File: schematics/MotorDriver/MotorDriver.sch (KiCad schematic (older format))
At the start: 13 parts, among them J1 I2C, J2 UART, J3 3V3IN, J4 9VIN, U1 ATmega328P-PU, U2 TB6612FNG, Y1 16MHz

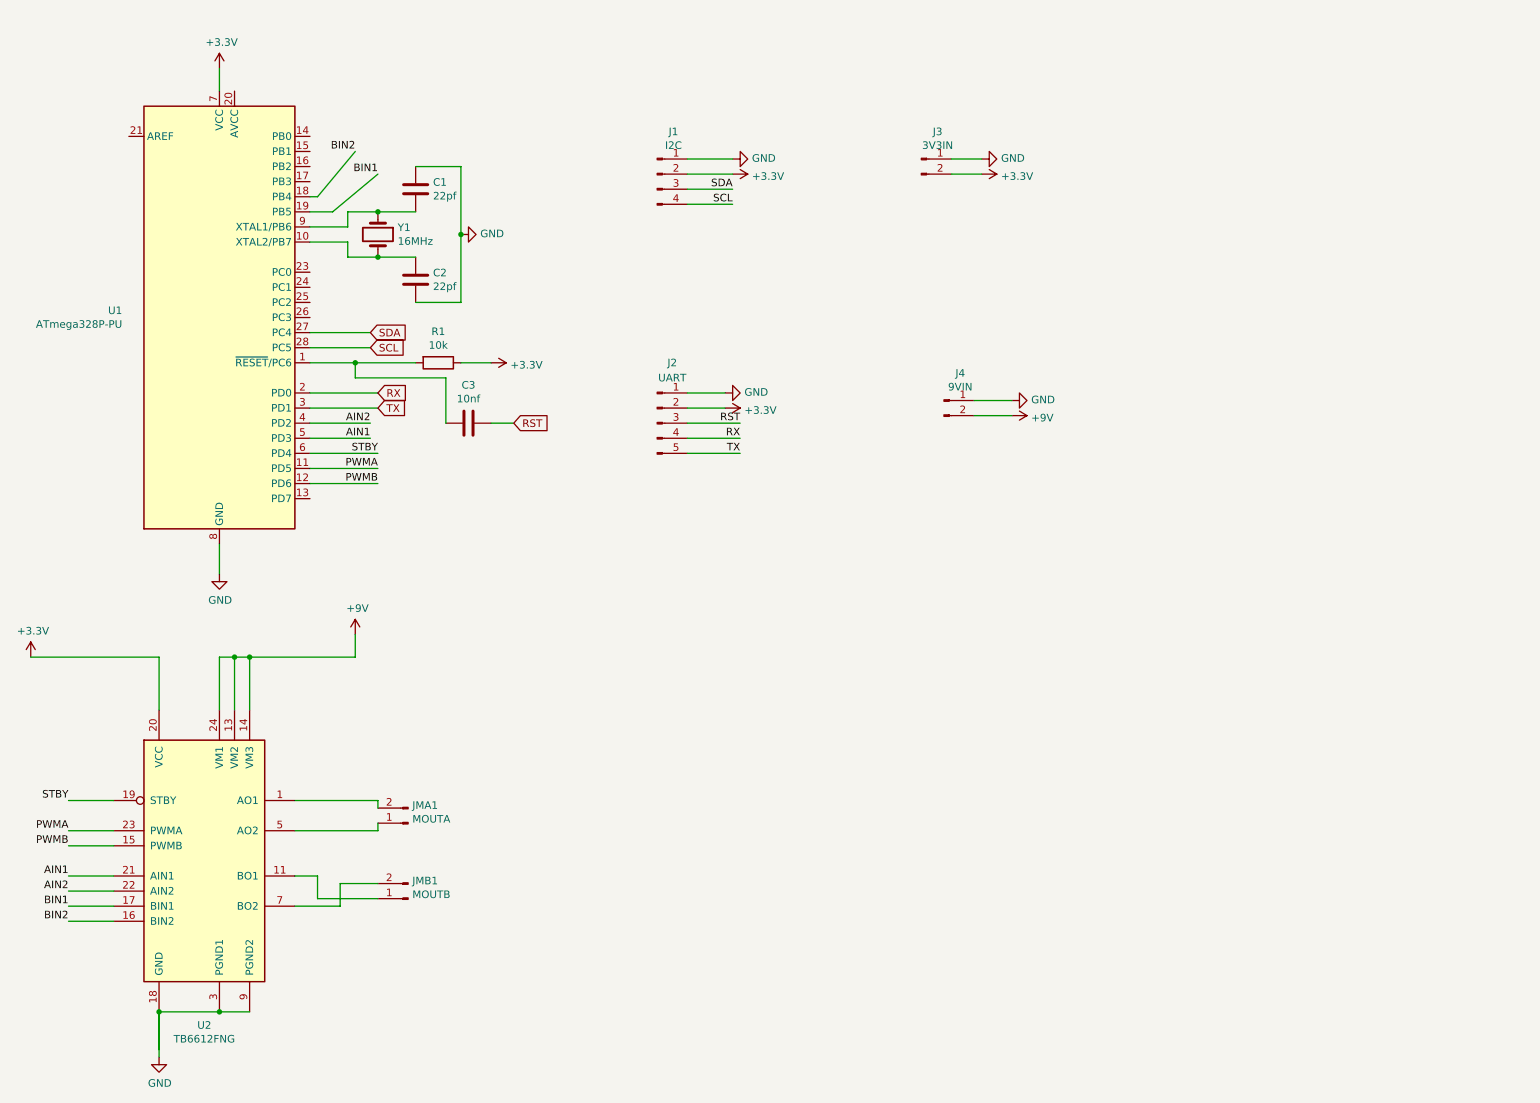
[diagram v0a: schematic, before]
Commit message: Added Caps
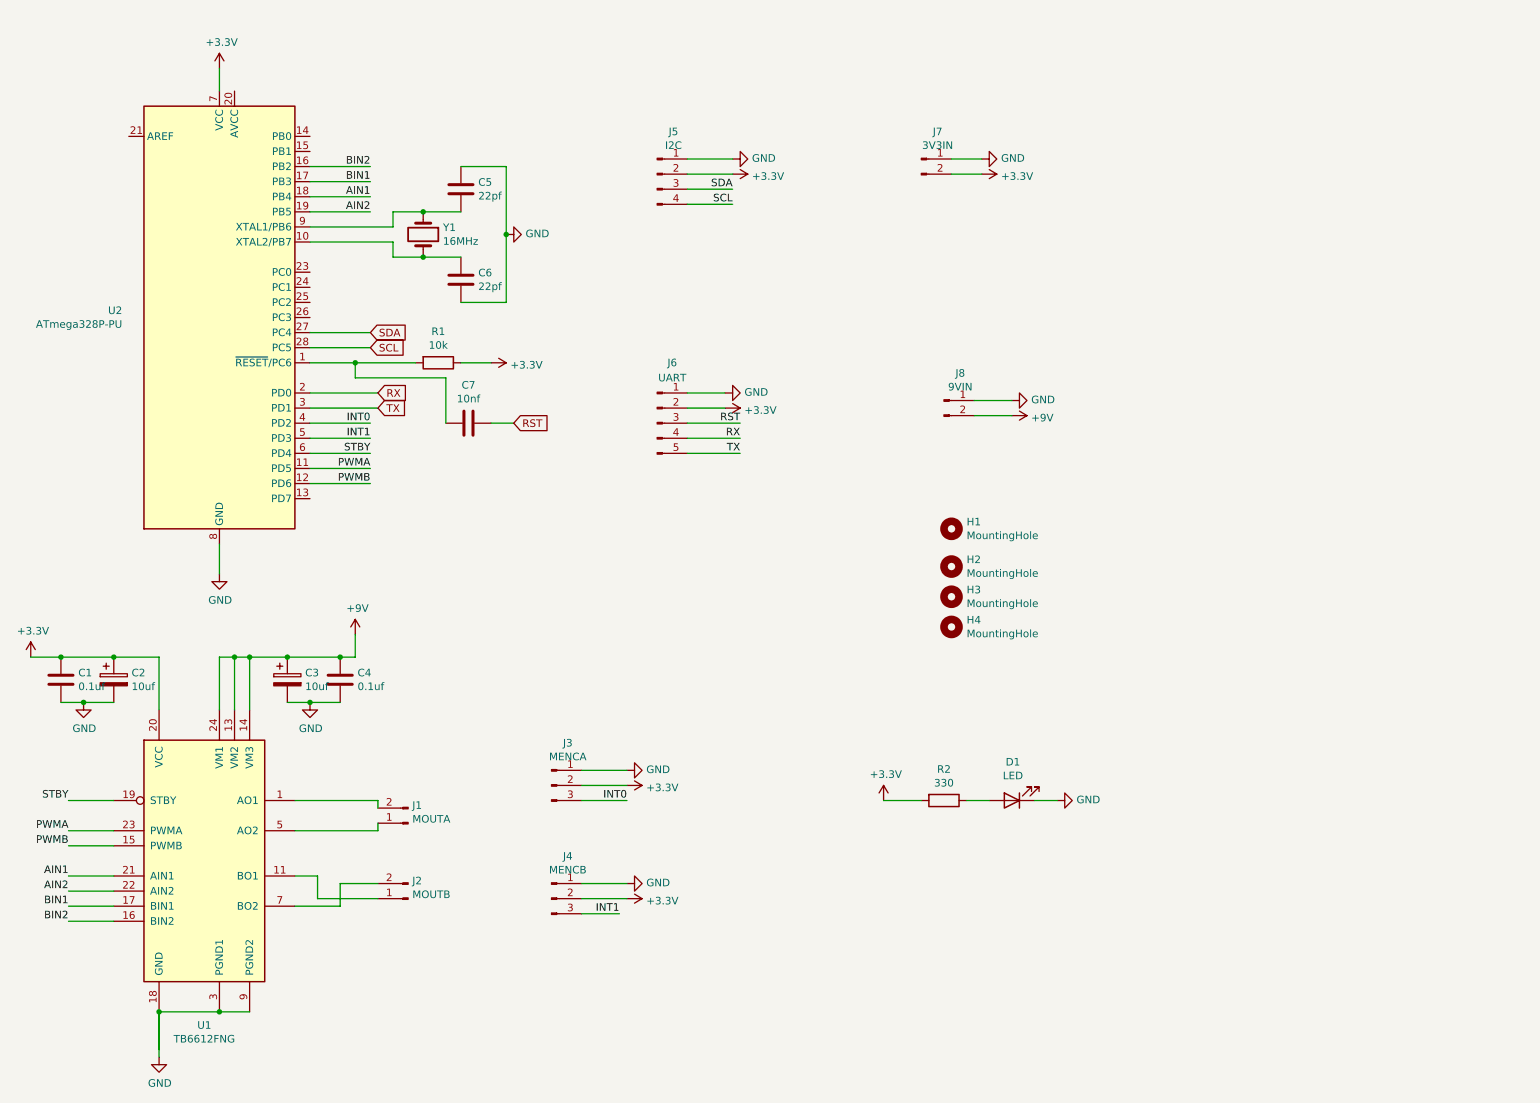
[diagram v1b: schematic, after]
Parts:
- added C1, C4: 0.1uf, Capacitor_SMD:C_1206_3216Metric, symbol Device:C
- added C2, C3: 10uf, Capacitor_SMD:CP_Elec_3x5.3, symbol Device:CP
- added D1: LED, LED_SMD:LED_1206_3216Metric, symbol Device:LED
- added H1, H2, H3, H4: MountingHole, MountingHole:MountingHole_2.5mm_Pad_TopBottom, symbol Mechanical:MountingHole
- added J3: MENCA, Connector_JST:JST_XH_B3B-XH-A_1x03_P2.50mm_Vertical, symbol Connector:Conn_01x03_Male
- added J4: MENCB, Connector_JST:JST_XH_B3B-XH-A_1x03_P2.50mm_Vertical, symbol Connector:Conn_01x03_Male
- added R2: 330, Resistor_SMD:R_1206_3216Metric, symbol Device:R
- renumbered C1 to C5, C2 to C6, C3 to C7, JMA1 to J1, JMB1 to J2, J1 to J5, J2 to J6, J3 to J7, J4 to J8, U2 to U1, U1 to U2
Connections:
- net +3V3: now also C1.1, C2.1, J3.2 (Pin_2), J4.2 (Pin_2), R2.2
- net +9V: now also C3.1, C4.1
- net AIN1: now also U2.18 (PB4); no longer U2.5 (PD3)
- net AIN2: now also U2.19 (PB5); no longer U2.4 (PD2)
- net BIN1: now also U2.17 (PB3); no longer U2.19 (PB5)
- net BIN2: now also U2.16 (PB2); no longer U2.18 (PB4)
- net GND: now also C1.2, C2.2, C3.2, C4.2, D1.1 (K), J3.1 (Pin_1), J4.1 (Pin_1)
- new net: D1.2 (A), R2.1
- new net INT0: J3.3 (Pin_3), U2.4 (PD2)
- new net INT1: J4.3 (Pin_3), U2.5 (PD3)
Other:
- moved on the sheet: C5, C6, Y1

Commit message: Changes
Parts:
- added C2: 100n, Capacitor_SMD:C_1206_3216Metric, symbol Device:C
- D1: value LED -> RED
- renumbered C2 to C3, C3 to C4, C4 to C5, C5 to C6, C6 to C7, C7 to C8, J5 to J1, J6 to J2, J8 to J3, J7 to J4, J1 to J5, J2 to J6, J3 to J7, J4 to J8
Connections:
- net +3V3: now also U2.20 (AVCC), C2.2
- net GND: now also C2.1
- net AO1: now reaches J5.2 (Pin_2), U1.1 (AO1), U1.2 (AO1)
- net BO1: now reaches J6.1 (Pin_1), U1.11 (BO1), U1.12 (BO1)
- net AO2: now reaches J5.1 (Pin_1), U1.5 (AO2), U1.6 (AO2)
- net BO2: now reaches J6.2 (Pin_2), U1.7 (BO2), U1.8 (BO2)
- no-connect marks 0 -> 8
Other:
- moved on the sheet: C4, C5, D1, H1, H2, H3, H4, J2, J3, J4, J5, J6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
